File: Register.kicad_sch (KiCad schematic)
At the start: 74 parts, among them U1 74LS173, U10 74LS245, U11 74LS245, U12 74LS245, U2 74LS173, U3 74LS173, U4 74LS173, U5 74LS173, U6 74LS173, U7 74LS173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

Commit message: Connect and organize Q lines
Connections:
- net Q17 is gone; now on an unnamed net: U5.3 (Q0)
- net Q18 is gone; now on an unnamed net: U5.4 (Q1)
- net Q19 is gone; now on an unnamed net: U5.5 (Q2)
- net Q20 is gone; now on an unnamed net: U5.6 (Q3)
- net Q21 is gone; now on an unnamed net: U6.3 (Q0)
- net Q22 is gone; now on an unnamed net: U6.4 (Q1)
- net Q23 is gone; now on an unnamed net: U6.5 (Q2)
- net Q24 is gone; now on an unnamed net: U6.6 (Q3)
- net Q25 is gone; now on an unnamed net: U7.3 (Q0)
- net Q26 is gone; now on an unnamed net: U7.4 (Q1)
- net Q27 is gone; now on an unnamed net: U7.5 (Q2)
- net Q28 is gone; now on an unnamed net: U7.6 (Q3)
- net Q29 is gone; now on an unnamed net: U8.3 (Q0)
- net Q30 is gone; now on an unnamed net: U8.4 (Q1)
- net Q31 is gone; now on an unnamed net: U8.5 (Q2)
- net +5V: now also U10.1 (A->B), U11.1 (A->B), U12.1 (A->B)
- net GND: now also U12.11 (B7), U12.9 (A7)
- net Q10: now also U10.3 (A1)
- net Q11: now also U10.4 (A2)
- net Q12: now also U10.5 (A3)
- net Q13: now also U10.6 (A4)
- net Q14: now also U10.7 (A5)
- net Q15: now also U10.8 (A6)
- net Q16: now also U10.9 (A7)
- net Q9: now also U10.2 (A0)
- net at U3.1 (Oe1): no longer U3.2 (Oe2)
- net Q1: no longer names the net of U1.3 (Q0), U9.2 (A0)
- net Q2: no longer names the net of U1.4 (Q1), U9.3 (A1)
- net Q3: no longer names the net of U1.5 (Q2), U9.4 (A2)
- net Q4: no longer names the net of U1.6 (Q3), U9.5 (A3)
- net Q5: no longer names the net of U2.3 (Q0), U9.6 (A4)
- net Q6: no longer names the net of U2.4 (Q1), U9.7 (A5)
- net Q7: no longer names the net of U2.5 (Q2), U9.8 (A6)
- net Q8: no longer names the net of U2.6 (Q3), U9.9 (A7)
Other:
- moved on the sheet: U1, U2, U3, U4, U5, U6, U7, U8, U9

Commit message: Added footprints
Added footprints for 74LS245s (SOIC 20, 12.8x7.5mm, 1.27mm pitch)
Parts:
- U10, U11, U12, U9: footprint (none) -> Package_SO:SOIC-20W_7.5x12.8mm_P1.27mm
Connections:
- net Q10: no longer names the net of U10.3 (A1), U3.4 (Q1)
- net Q11: no longer names the net of U10.4 (A2), U3.5 (Q2)
- net Q12: no longer names the net of U10.5 (A3), U3.6 (Q3)
- net Q13: no longer names the net of U10.6 (A4), U4.3 (Q0)
- net Q14: no longer names the net of U10.7 (A5), U4.4 (Q1)
- net Q15: no longer names the net of U10.8 (A6), U4.5 (Q2)
- net Q16: no longer names the net of U10.9 (A7), U4.6 (Q3)
- net Q9: no longer names the net of U10.2 (A0), U3.3 (Q0)
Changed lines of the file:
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@@
-    (effects (font (size 1.27 1.27)) (justify right bottom))
-  )
-  (label "Q10" (at 227.33 53.34 270) (fields_autoplaced)
     (effects (font (size 1.27 1.27)) (justify right bottom))
   )
@@
     (effects (font (size 1.27 1.27)) (justify right bottom))
   )
-  (label "Q13" (at 219.71 53.34 270) (fields_autoplaced)
-    (effects (font (size 1.27 1.27)) (justify right bottom))
-  )
   (label "LED11" (at 104.14 161.29 0) (fields_autoplaced)
     (effects (font (size 1.27 1.27)) (justify left bottom))
@@
     (effects (font (size 1.27 1.27)) (justify right bottom))
   )
-  (label "Q9" (at 229.87 53.34 270) (fields_autoplaced)
-    (effects (font (size 1.27 1.27)) (justify right bottom))
-  )
   (label "DR" (at 106.68 15.24 270) (fields_autoplaced)
     (effects (font (size 1.27 1.27)) (justify right bottom))
@@
     (effects (font (size 1.27 1.27)) (justify left bottom))
   )
-  (label "Q14" (at 217.17 53.34 270) (fields_autoplaced)
-    (effects (font (size 1.27 1.27)) (justify right bottom))
-  )
   (label "DR" (at 236.22 86.36 270) (fields_autoplaced)
     (effects (font (size 1.27 1.27)) (justify right bottom))
@@
     (effects (font (size 1.27 1.27)) (justify left bottom))
   )
-  (label "Q11" (at 224.79 53.34 270) (fields_autoplaced)
-    (effects (font (size 1.27 1.27)) (justify right bottom))
-  )
   (label "D17" (at 74.93 91.44 270) (fields_autoplaced)
     (effects (font (size 1.27 1.27)) (justify right bottom))
@@
     (effects (font (size 1.27 1.27)) (justify right bottom))
   )
-  (label "Q12" (at 222.25 53.34 270) (fields_autoplaced)
-    (effects (font (size 1.27 1.27)) (justify right bottom))
-  )
   (label "D22" (at 125.73 91.44 270) (fields_autoplaced)
     (effects (font (size 1.27 1.27)) (justify right bottom))
@@
     (effects (font (size 1.27 1.27)) (justify right bottom))
   )
-  (label "Q16" (at 212.09 53.34 270) (fields_autoplaced)
-    (effects (font (size 1.27 1.27)) (justify right bottom))
-  )
   (label "LED30" (at 130.81 180.34 0) (fields_autoplaced)
     (effects (font (size 1.27 1.27)) (justify left bottom))
@@
   )
   (label "DR" (at 182.88 13.97 270) (fields_autoplaced)
-    (effects (font (size 1.27 1.27)) (justify right bottom))
-  )
-  (label "Q15" (at 214.63 53.34 270) (fields_autoplaced)
     (effects (font (size 1.27 1.27)) (justify right bottom))
   )
@@
       (effects (font (size 1.27 1.27)) (justify left))
     )
-    (property "Footprint" "" (at 217.17 66.04 0)
+    (property "Footprint" "Package_SO:SOIC-20W_7.5x12.8mm_P1.27mm" (at 217.17 66.04 0)
       (effects (font (size 1.27 1.27)) hide)
     )
@@
       (effects (font (size 1.27 1.27)))
     )
-    (property "Footprint" "" (at 87.63 139.7 0)
+    (property "Footprint" "Package_SO:SOIC-20W_7.5x12.8mm_P1.27mm" (at 87.63 139.7 0)
       (effects (font (size 1.27 1.27)) hide)
     )
@@
       (effects (font (size 1.27 1.27)))
     )
-    (property "Footprint" "" (at 215.9 138.43 0)
+    (property "Footprint" "Package_SO:SOIC-20W_7.5x12.8mm_P1.27mm" (at 215.9 138.43 0)
       (effects (font (size 1.27 1.27)) hide)
     )
@@
       (effects (font (size 1.27 1.27)))
     )
-    (property "Footprint" "" (at 88.9 67.31 0)
-      (effects (font (size 1.27 1.27)) hide)
-    )
+    (property "Footprint" "Package_SO:SOIC-20W_7.5x12.8mm_P1.27mm" (at 88.9 67.31 0)
+      (effects (font (size 1.27 1.27)) hide)
+    )

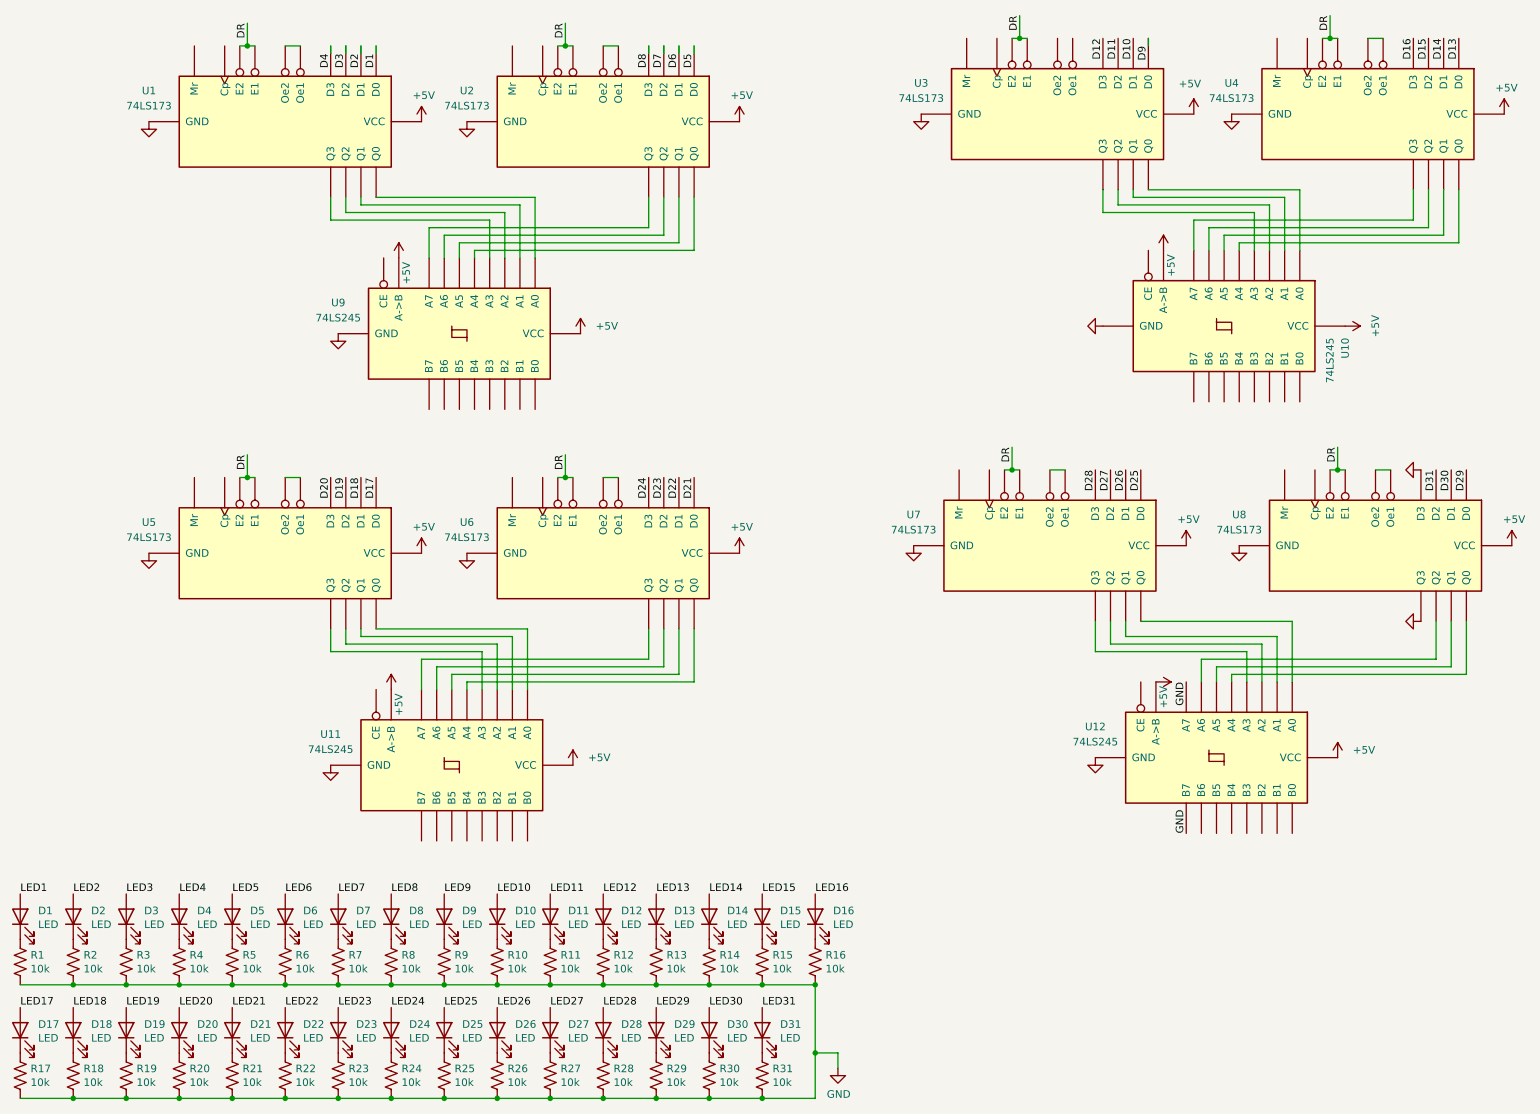
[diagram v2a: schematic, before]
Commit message: Fixed wiring issues
The registers weren't connected to the bus xcvr correctly, so I rewired the connections between them.  The new connections allow for a much better physical layout.
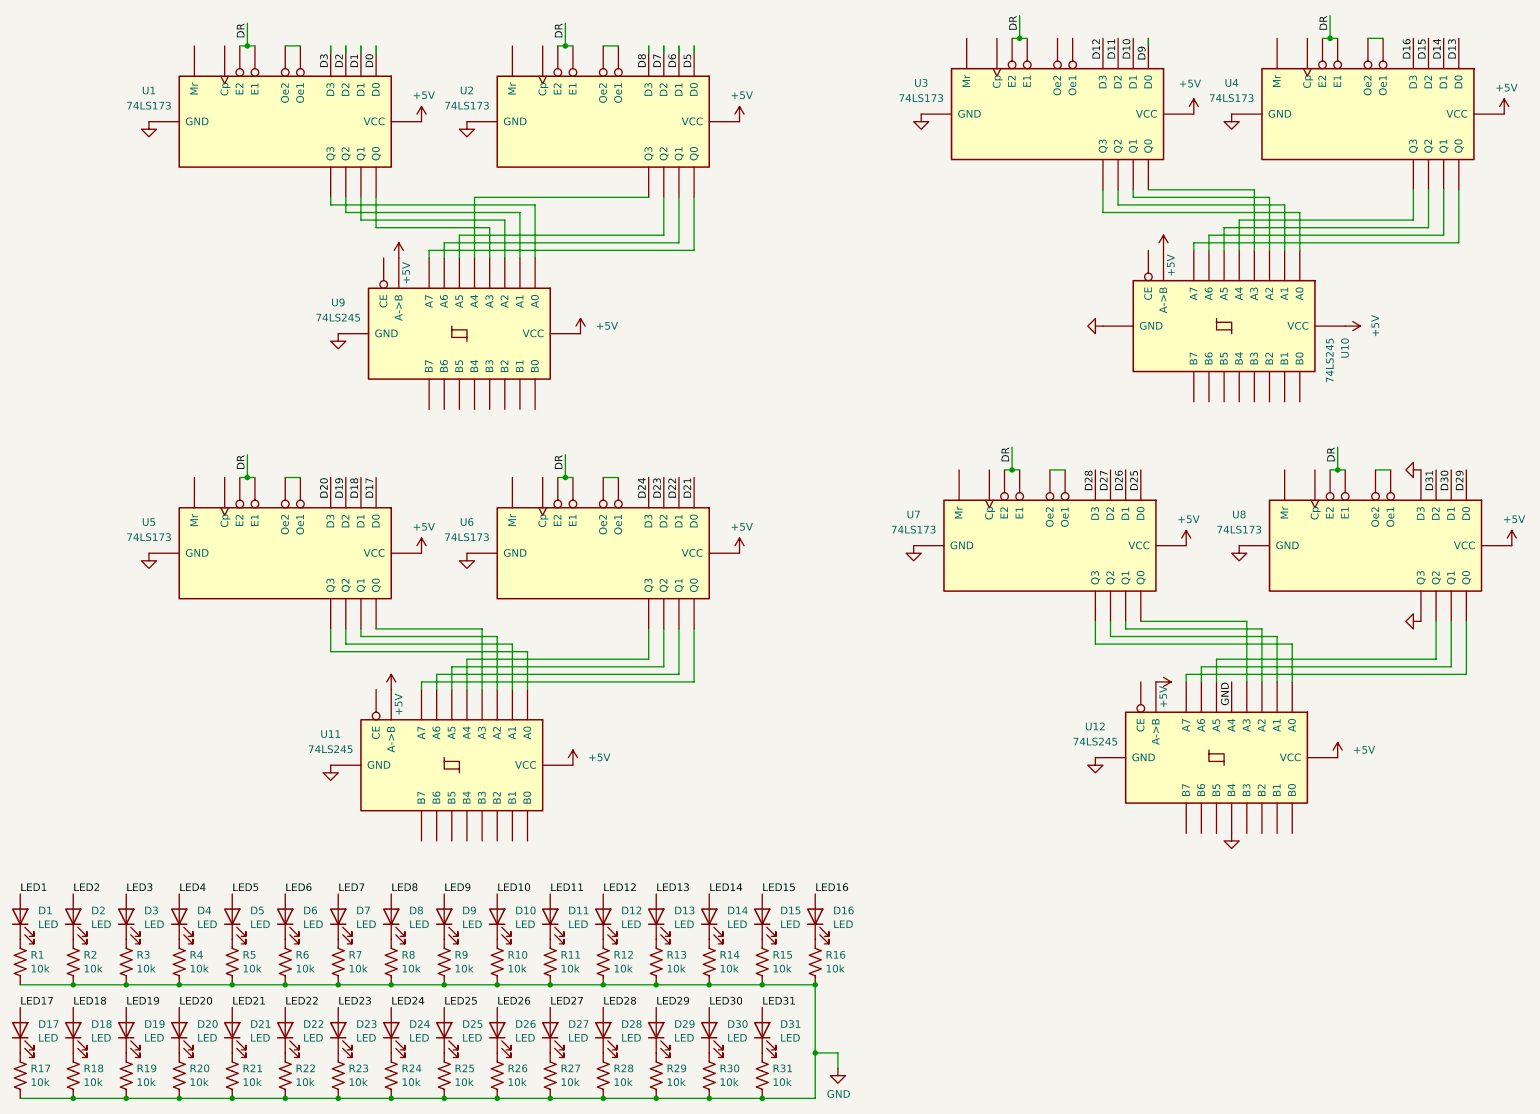
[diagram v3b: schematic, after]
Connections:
- net D4 is gone; now on net D3: U1.11 (D3)
- net D1: now also U1.13 (D1); no longer U1.14 (D0)
- net D2: now also U1.12 (D2); no longer U1.13 (D1)
- net D3: no longer U1.12 (D2)
- net GND: now also U12.14 (B4), U12.6 (A4); no longer U12.11 (B7), U12.9 (A7)
- net at U2.3 (Q0): now also U9.9 (A7); no longer U9.6 (A4)
- net at U2.4 (Q1): now also U9.8 (A6); no longer U9.7 (A5)
- net at U2.5 (Q2): now also U9.7 (A5); no longer U9.8 (A6)
- net at U2.6 (Q3): now also U9.6 (A4); no longer U9.9 (A7)
- net at U1.3 (Q0): now also U9.5 (A3); no longer U9.2 (A0)
- net at U1.4 (Q1): now also U9.4 (A2); no longer U9.3 (A1)
- net at U1.5 (Q2): now also U9.3 (A1); no longer U9.4 (A2)
- net at U1.6 (Q3): now also U9.2 (A0); no longer U9.5 (A3)
- net at U10.2 (A0): now also U3.6 (Q3); no longer U3.3 (Q0)
- net at U10.3 (A1): now also U3.5 (Q2); no longer U3.4 (Q1)
- net at U10.4 (A2): now also U3.4 (Q1); no longer U3.5 (Q2)
- net at U10.5 (A3): now also U3.3 (Q0); no longer U3.6 (Q3)
- net at U10.6 (A4): now also U4.6 (Q3); no longer U4.3 (Q0)
- net at U10.7 (A5): now also U4.5 (Q2); no longer U4.4 (Q1)
- net at U10.8 (A6): now also U4.4 (Q1); no longer U4.5 (Q2)
- net at U10.9 (A7): now also U4.3 (Q0); no longer U4.6 (Q3)
- net at U11.2 (A0): now also U5.6 (Q3); no longer U5.3 (Q0)
- net at U11.3 (A1): now also U5.5 (Q2); no longer U5.4 (Q1)
- net at U11.4 (A2): now also U5.4 (Q1); no longer U5.5 (Q2)
- net at U11.5 (A3): now also U5.3 (Q0); no longer U5.6 (Q3)
- net at U11.6 (A4): now also U6.6 (Q3); no longer U6.3 (Q0)
- net at U11.7 (A5): now also U6.5 (Q2); no longer U6.4 (Q1)
- net at U11.8 (A6): now also U6.4 (Q1); no longer U6.5 (Q2)
- net at U11.9 (A7): now also U6.3 (Q0); no longer U6.6 (Q3)
- net at U12.2 (A0): now also U7.6 (Q3); no longer U7.3 (Q0)
- net at U12.3 (A1): now also U7.5 (Q2); no longer U7.4 (Q1)
- net at U12.4 (A2): now also U7.4 (Q1); no longer U7.5 (Q2)
- net at U12.5 (A3): now also U7.3 (Q0); no longer U7.6 (Q3)
- net at U8.3 (Q0): now also U12.9 (A7); no longer U12.6 (A4)
- net at U12.7 (A5): now also U8.5 (Q2); no longer U8.4 (Q1)
- net at U12.8 (A6): now also U8.4 (Q1); no longer U8.5 (Q2)
- new net D0: U1.14 (D0)
